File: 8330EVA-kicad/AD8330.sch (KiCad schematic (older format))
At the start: 2 parts, among them U1 AD8131, U3 AD8330

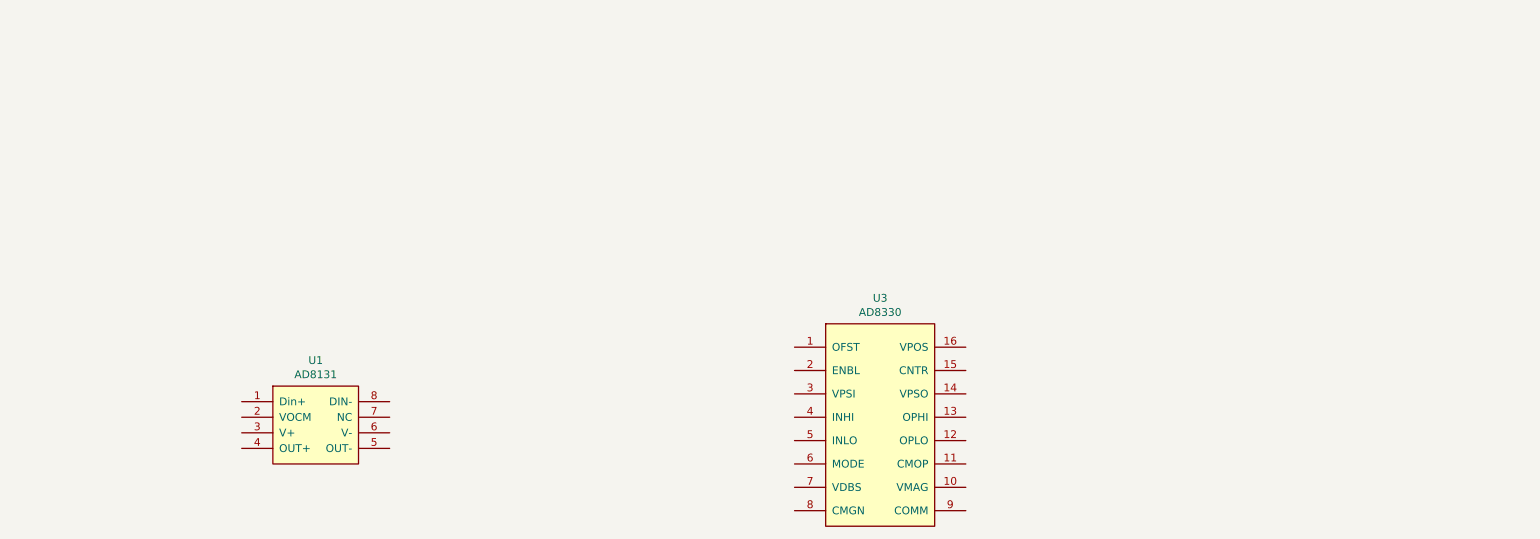
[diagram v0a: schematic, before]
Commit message: 完成AD8131单端转差分放大原理图绘制
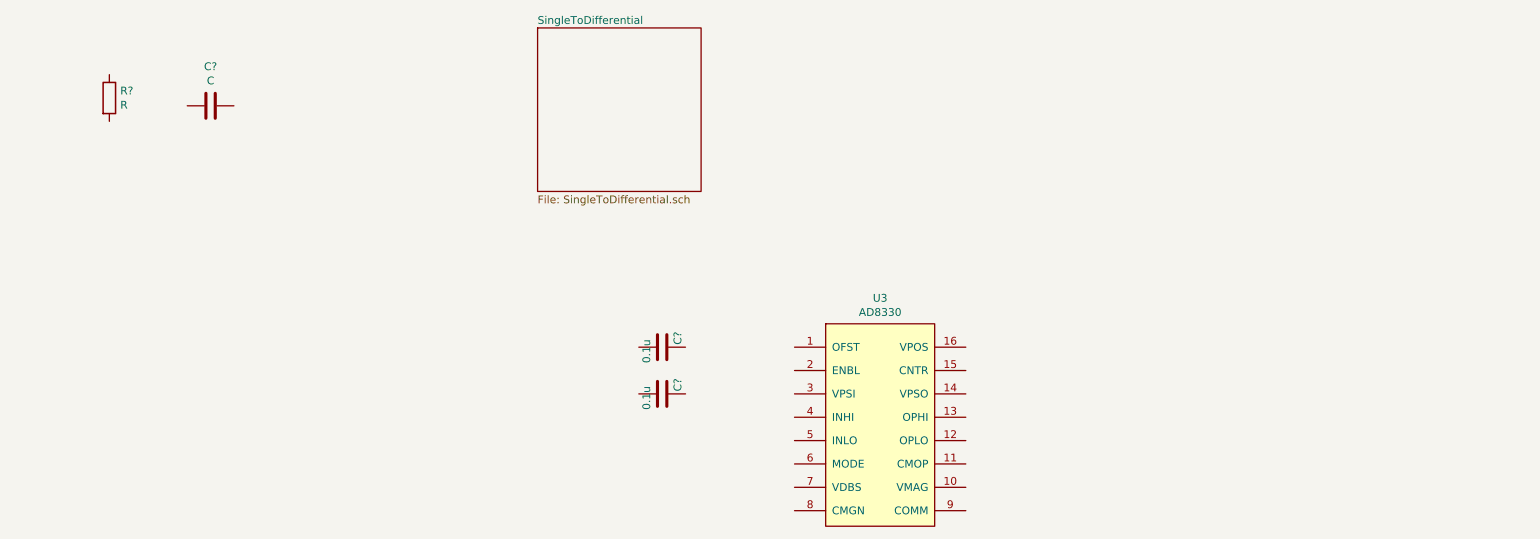
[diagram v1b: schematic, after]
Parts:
- removed U1: AD8131, Package_SO:SOIC-8_3.9x4.9mm_P1.27mm, symbol 8330_EVA-extra:AD8131
- added C?: C, symbol Device:C
- added C? (x2): 0.1u, symbol Device:C
- added R?: R, symbol Device:R
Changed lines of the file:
@@
 $Descr A4 11693 8268
 encoding utf-8
-Sheet 3 3
+Sheet 3 5
 Title ""
 Date ""
@@
 $EndComp
 $Comp
-L 8330_EVA-extra:AD8131 U1
-U 1 1 5BF81695
-P 2850 3250
-F 0 "U1" H 2825 3665 50  0000 C CNN
-F 1 "AD8131" H 2825 3574 50  0000 C CNN
-F 2 "Package_SO:SOIC-8_3.9x4.9mm_P1.27mm" H 3000 2850 50  0001 C CNN
-F 3 "https://www.analog.com/media/en/technical-documentation/data-sheets/AD8131.pdf" H 3000 2750 50  0001 C CNN
-	1    2850 3250
+L Device:R R?
+U 1 1 5BF9B361
+P 1500 1150
+F 0 "R?" H 1570 1196 50  0000 L CNN
+F 1 "R" H 1570 1105 50  0000 L CNN
+F 2 "" V 1430 1150 50  0001 C CNN
+F 3 "~" H 1500 1150 50  0001 C CNN
+	1    1500 1150
 	1    0    0    -1
 $EndComp
+$Comp
+L Device:C C?
+U 1 1 5BF9B6CC
+P 2150 1200
+F 0 "C?" V 1898 1200 50  0000 C CNN
+F 1 "C" V 1989 1200 50  0000 C CNN
+F 2 "" H 2188 1050 50  0001 C CNN
+F 3 "~" H 2150 1200 50  0001 C CNN
+	1    2150 1200
+	0    1    1    0
+$EndComp
+$Comp
+L Device:C C?
+U 1 1 5BFA5F5C
+P 5050 2750
+F 0 "C?" H 5150 2650 50  0000 R CNN
+F 1 "0.1u" H 5100 2850 50  0000 R CNN
+F 2 "" H 5088 2600 50  0001 C CNN
+F 3 "~" H 5050 2750 50  0001 C CNN
+	1    5050 2750
+	0    -1   -1   0
+$EndComp
+$Comp
+L Device:C C?
+U 1 1 5BFA682C
+P 5050 3050
+F 0 "C?" H 5150 2950 50  0000 R CNN
+F 1 "0.1u" H 5100 3150 50  0000 R CNN
+F 2 "" H 5088 2900 50  0001 C CNN
+F 3 "~" H 5050 3050 50  0001 C CNN
+	1    5050 3050
+	0    -1   -1   0
+$EndComp
+$Sheet
+S 4250 700  1050 1050
+U 5BFB4FFD
+F0 "SingleToDifferential" 50
+F1 "SingleToDifferential.sch" 50
+$EndSheet
 $EndSCHEMATC

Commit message: 完成AD8330 VGA电路原理图的绘制
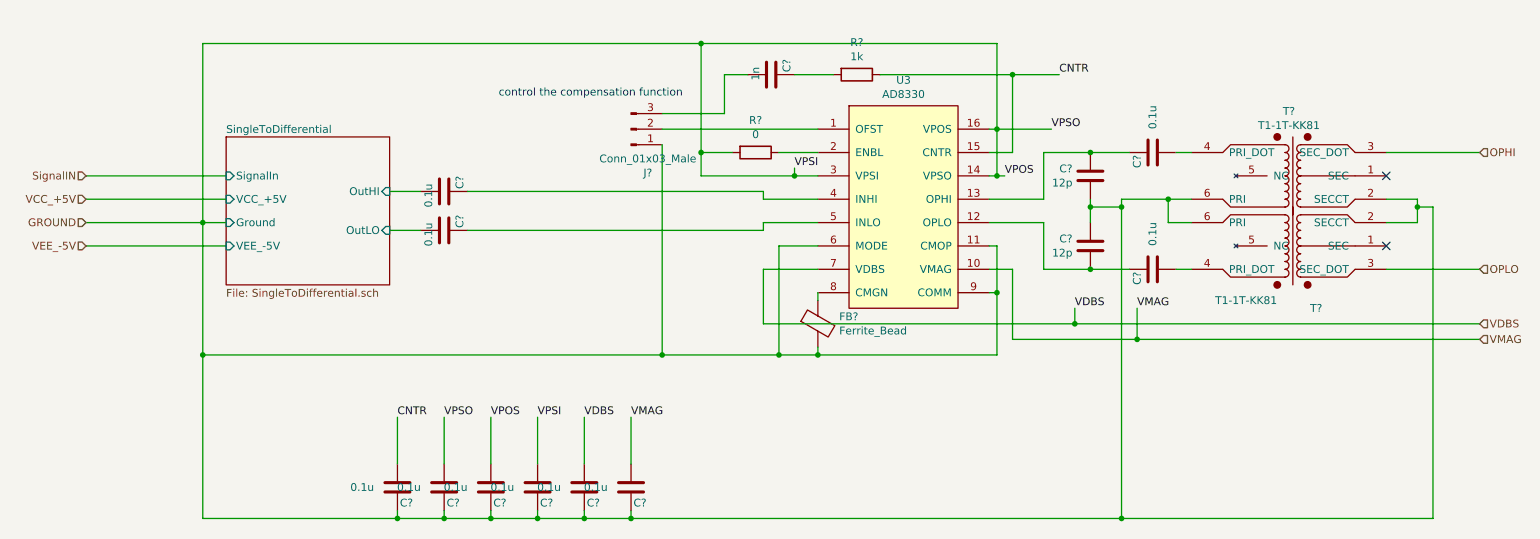
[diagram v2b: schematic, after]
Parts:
- removed C?: C, symbol Device:C
- removed C?: 0.1u, symbol Device:C
- added C? (x9): 0.1u, symbol Device:C
- added C? (x2): 12p, symbol Device:C
- added C?: 1n, symbol Device:C
- added FB?: Ferrite_Bead, symbol Device:Ferrite_Bead
- added J?: Conn_01x03_Male, symbol Connector:Conn_01x03_Male
- added R?: 1k, symbol Device:R
- added T? (x2): T1-1T-KK81, symbol 8330_EVA-extra:T1-1T-KK81
- R?: value R -> 0
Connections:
- net at U3.1 (OFST): now also J?.2 (Pin_2)
- net VMAG: now reaches U3.10 (VMAG)
- net VMAG: now also C?.1
- net GROUND: now reaches U3.11 (CMOP)
- net GROUND: now also R?.2, U3.14 (VPSO), U3.16 (VPOS), U3.3 (VPSI), U3.6 (MODE), U3.9 (COMM), C?.1, C?.1, C?.1, C?.1, C?.2, C?.2, C?.2, C?.2, C?.2, C?.2, C?.2, FB?.2, J?.1 (Pin_1), T?.2 (SECCT), T?.2 (SECCT), T?.6 (PRI), T?.6 (PRI)
- net at U3.12 (OPLO): now also C?.1, C?.2
- net at U3.13 (OPHI): now also C?.2, C?.2
- net CNTR: now reaches U3.15 (CNTR)
- net CNTR: now also C?.1, R?.1
- net at U3.2 (ENBL): now also R?.1
- net at U3.4 (INHI): now also C?.2
- net at U3.5 (INLO): now also C?.2
- net VDBS: now reaches U3.7 (VDBS)
- net VDBS: now also C?.1
- net at U3.8 (CMGN): now also FB?.1
- net SingleToDifferential/OutLO: now reaches C?.1
- new net: C?.1, T?.4 (PRI_DOT) (x2)
- new net: C?.1, J?.3 (Pin_3)
- new net: C?.2, R?.2
- new net OPHI: T?.3 (SEC_DOT)
- new net OPLO: T?.3 (SEC_DOT)
- new net SingleToDifferential/OutHI: C?.1
- no-connect marks 0 -> 2
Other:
- note added: "control the compensation function\n"
- moved on the sheet: C?, R?, U3

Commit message: 修复若干ERC未连接错误
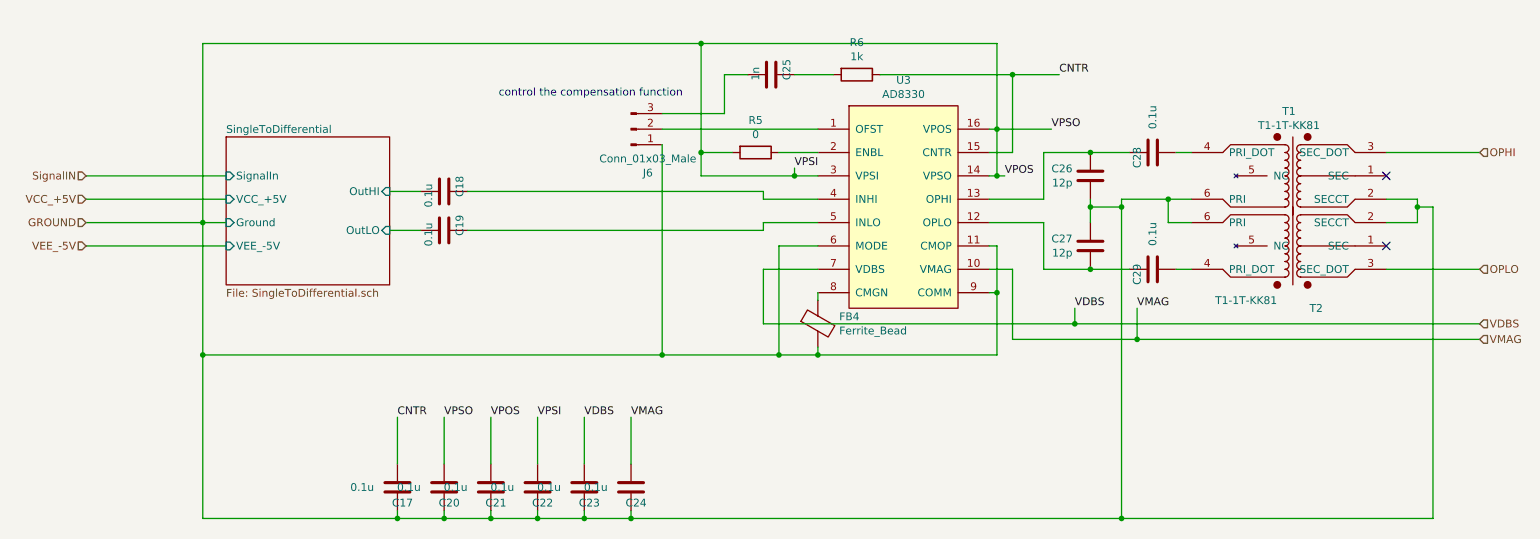
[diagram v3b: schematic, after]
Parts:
- gave numbers to parts that had none: 19
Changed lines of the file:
@@
 $EndComp
 $Comp
-L Device:R R?
+L Device:R R5
 U 1 1 5BF9B361
 P 5650 1500
-F 0 "R?" V 5443 1500 50  0000 C CNN
+F 0 "R5" V 5443 1500 50  0000 C CNN
 F 1 "0" V 5534 1500 50  0000 C CNN
 F 2 "" V 5580 1500 50  0001 C CNN
@@
 $EndComp
 $Comp
-L Device:C C?
+L Device:C C19
 U 1 1 5BFA682C
 P 3650 2000
-F 0 "C?" H 3750 1900 50  0000 R CNN
+F 0 "C19" H 3750 1900 50  0000 R CNN
 F 1 "0.1u" H 3700 2100 50  0000 R CNN
 F 2 "" H 3688 1850 50  0001 C CNN
@@
 	5700 1950 6050 1950
 $Comp
-L Device:C C?
+L Device:C C18
 U 1 1 5BFC8B3F
 P 3650 1750
-F 0 "C?" H 3750 1650 50  0000 R CNN
+F 0 "C18" H 3750 1650 50  0000 R CNN
 F 1 "0.1u" H 3700 1850 50  0000 R CNN
 F 2 "" H 3688 1600 50  0001 C CNN
@@
 	7500 1950 7500 2250
 $Comp
-L Device:C C?
+L Device:C C26
 U 1 1 5BFD0258
 P 7800 1650
-F 0 "C?" H 7685 1604 50  0000 R CNN
+F 0 "C26" H 7685 1604 50  0000 R CNN
 F 1 "12p" H 7685 1695 50  0000 R CNN
 F 2 "" H 7838 1500 50  0001 C CNN
@@
 $EndComp
 $Comp
-L Device:C C?
+L Device:C C27
 U 1 1 5BFD06D1
 P 7800 2100
-F 0 "C?" H 7685 2054 50  0000 R CNN
+F 0 "C27" H 7685 2054 50  0000 R CNN
 F 1 "12p" H 7685 2145 50  0000 R CNN
 F 2 "" H 7838 1950 50  0001 C CNN
@@
 	7800 1850 7800 1950
 $Comp
-L 8330_EVA-extra:T1-1T-KK81 T?
+L 8330_EVA-extra:T1-1T-KK81 T1
 U 1 1 5BFDF9EF
 P 9100 1650
-F 0 "T?" H 9075 2065 50  0000 C CNN
+F 0 "T1" H 9075 2065 50  0000 C CNN
 F 1 "T1-1T-KK81" H 9075 1974 50  0000 C CNN
 F 2 "" H 9690 1690 50  0001 C CNN
@@
 $EndComp
 $Comp
-L 8330_EVA-extra:T1-1T-KK81 T?
+L 8330_EVA-extra:T1-1T-KK81 T2
 U 1 1 5BFE14B7
 P 9100 2100
-F 0 "T?" H 9250 2500 50  0000 C CNN
+F 0 "T2" H 9250 2500 50  0000 C CNN
 F 1 "T1-1T-KK81" H 8800 2450 50  0000 C CNN
 F 2 "" H 9690 2140 50  0001 C CNN
@@
 Connection ~ 8000 1850
 Wire Wire Line
-	9700 1800 9900 1800
-Wire Wire Line
 	9900 1950 9700 1950
 Wire Wire Line
@@
 Connection ~ 7200 1350
 $Comp
-L Connector:Conn_01x03_Male J?
+L Connector:Conn_01x03_Male J6
 U 1 1 5C005F86
 P 4850 1350
-F 0 "J?" H 4958 1631 50  0000 C CNN
+F 0 "J6" H 4958 1631 50  0000 C CNN
 F 1 "Conn_01x03_Male" H 4958 1540 50  0000 C CNN
 F 2 "" H 4850 1350 50  0001 C CNN
@@
 	5050 1450 5050 2800
 $Comp
-L Device:R R?
+L Device:R R6
 U 1 1 5C01343E
 P 6300 1000
-F 0 "R?" V 6093 1000 50  0000 C CNN
+F 0 "R6" V 6093 1000 50  0000 C CNN
 F 1 "1k" V 6184 1000 50  0000 C CNN
 F 2 "" V 6230 1000 50  0001 C CNN
@@
 $EndComp
 $Comp
-L Device:C C?
+L Device:C C25
 U 1 1 5C01399A
 P 5750 1000
-F 0 "C?" H 5850 900 50  0000 R CNN
+F 0 "C25" H 5850 900 50  0000 R CNN
 F 1 "1n" H 5800 1100 50  0000 R CNN
 F 2 "" H 5788 850 50  0001 C CNN
@@
 control the compensation function\n
 $Comp
-L Device:Ferrite_Bead FB?
+L Device:Ferrite_Bead FB4
 U 1 1 5C01A12D
 P 6050 2600
-F 0 "FB?" H 6187 2646 50  0000 L CNN
+F 0 "FB4" H 6187 2646 50  0000 L CNN
 F 1 "Ferrite_Bead" H 6187 2555 50  0000 L CNN
 F 2 "" V 5980 2600 50  0001 C CNN
@@
 	5900 1650 6050 1650
 $Comp
-L Device:C C?
+L Device:C C21
 U 1 1 5C02ECCD
 P 3950 3650
-F 0 "C?" H 4050 3550 50  0000 R CNN
+F 0 "C21" H 4050 3550 50  0000 R CNN
 F 1 "0.1u" H 3800 3650 50  0000 R CNN
 F 2 "" H 3988 3500 50  0001 C CNN
@@
 $EndComp
 $Comp
-L Device:C C?
+L Device:C C22
 U 1 1 5C030FD6
 P 4250 3650
-F 0 "C?" H 4350 3550 50  0000 R CNN
+F 0 "C22" H 4350 3550 50  0000 R CNN
 F 1 "0.1u" H 4100 3650 50  0000 R CNN
 F 2 "" H 4288 3500 50  0001 C CNN
@@
 $EndComp
 $Comp
-L Device:C C?
+L Device:C C23
 U 1 1 5C0312A5
 P 4550 3650
-F 0 "C?" H 4650 3550 50  0000 R CNN
+F 0 "C23" H 4650 3550 50  0000 R CNN
 F 1 "0.1u" H 4400 3650 50  0000 R CNN
 F 2 "" H 4588 3500 50  0001 C CNN
@@
 $EndComp
 $Comp
-L Device:C C?
+L Device:C C24
 U 1 1 5C031714
 P 4850 3650
-F 0 "C?" H 4950 3550 50  0000 R CNN
+F 0 "C24" H 4950 3550 50  0000 R CNN
 F 1 "0.1u" H 4700 3650 50  0000 R CNN
 F 2 "" H 4888 3500 50  0001 C CNN
@@
 $EndComp
 $Comp
-L Device:C C?
+L Device:C C20
 U 1 1 5C031A2F
 P 3650 3650
-F 0 "C?" H 3750 3550 50  0000 R CNN
+F 0 "C20" H 3750 3550 50  0000 R CNN
 F 1 "0.1u" H 3500 3650 50  0000 R CNN
 F 2 "" H 3688 3500 50  0001 C CNN
@@
 $EndComp
 $Comp
-L Device:C C?
+L Device:C C17
 U 1 1 5C031D96
 P 3350 3650
-F 0 "C?" H 3450 3550 50  0000 R CNN
+F 0 "C17" H 3450 3550 50  0000 R CNN
 F 1 "0.1u" H 3200 3650 50  0000 R CNN
 F 2 "" H 3388 3500 50  0001 C CNN
@@
 NoConn ~ 9700 2100
 $Comp
-L Device:C C?
+L Device:C C28
 U 1 1 5C087144
 P 8200 1500
-F 0 "C?" H 8300 1400 50  0000 R CNN
+F 0 "C28" H 8300 1400 50  0000 R CNN
 F 1 "0.1u" H 8050 1500 50  0000 R CNN
 F 2 "" H 8238 1350 50  0001 C CNN
@@
 Connection ~ 7800 1500
 $Comp
-L Device:C C?
+L Device:C C29
 U 1 1 5C0A02D1
 P 8200 2250
-F 0 "C?" H 8300 2150 50  0000 R CNN
+F 0 "C29" H 8300 2150 50  0000 R CNN
 F 1 "0.1u" H 8050 2250 50  0000 R CNN
 F 2 "" H 8238 2100 50  0001 C CNN
@@
 EndData
 $EndBitmap
+Wire Wire Line
+	9700 1800 9900 1800
 $EndSCHEMATC

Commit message: 为变压器制作封装
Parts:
- C17, C18, C19, C20, C21, C22, C23, C24, C25, C26, C27, C28, C29: footprint (none) -> Capacitor_SMD:C_0603_1608Metric_Pad1.05x0.95mm_HandSolder
- FB4: footprint (none) -> Inductor_SMD:L_0805_2012Metric_Pad1.15x1.40mm_HandSolder
- J6: footprint (none) -> Connector_PinHeader_2.54mm:PinHeader_1x03_P2.54mm_Vertical
- R5, R6: footprint (none) -> Resistor_SMD:R_0805_2012Metric_Pad1.15x1.40mm_HandSolder
- T1, T2: footprint (none) -> 8330EVA-footprint-extra:Mini_Circuit_RF_Transformer_SO6
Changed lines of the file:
@@
 F 0 "R5" V 5443 1500 50  0000 C CNN
 F 1 "0" V 5534 1500 50  0000 C CNN
-F 2 "" V 5580 1500 50  0001 C CNN
+F 2 "Resistor_SMD:R_0805_2012Metric_Pad1.15x1.40mm_HandSolder" V 5580 1500 50  0001 C CNN
 F 3 "~" H 5650 1500 50  0001 C CNN
 	1    5650 1500
@@
 F 0 "C19" H 3750 1900 50  0000 R CNN
 F 1 "0.1u" H 3700 2100 50  0000 R CNN
-F 2 "" H 3688 1850 50  0001 C CNN
+F 2 "Capacitor_SMD:C_0603_1608Metric_Pad1.05x0.95mm_HandSolder" H 3688 1850 50  0001 C CNN
 F 3 "~" H 3650 2000 50  0001 C CNN
 	1    3650 2000
@@
 F 0 "C18" H 3750 1650 50  0000 R CNN
 F 1 "0.1u" H 3700 1850 50  0000 R CNN
-F 2 "" H 3688 1600 50  0001 C CNN
+F 2 "Capacitor_SMD:C_0603_1608Metric_Pad1.05x0.95mm_HandSolder" H 3688 1600 50  0001 C CNN
 F 3 "~" H 3650 1750 50  0001 C CNN
 	1    3650 1750
@@
 F 0 "C26" H 7685 1604 50  0000 R CNN
 F 1 "12p" H 7685 1695 50  0000 R CNN
-F 2 "" H 7838 1500 50  0001 C CNN
+F 2 "Capacitor_SMD:C_0603_1608Metric_Pad1.05x0.95mm_HandSolder" H 7838 1500 50  0001 C CNN
 F 3 "~" H 7800 1650 50  0001 C CNN
 	1    7800 1650
@@
 F 0 "C27" H 7685 2054 50  0000 R CNN
 F 1 "12p" H 7685 2145 50  0000 R CNN
-F 2 "" H 7838 1950 50  0001 C CNN
+F 2 "Capacitor_SMD:C_0603_1608Metric_Pad1.05x0.95mm_HandSolder" H 7838 1950 50  0001 C CNN
 F 3 "~" H 7800 2100 50  0001 C CNN
 	1    7800 2100
@@
 F 0 "T1" H 9075 2065 50  0000 C CNN
 F 1 "T1-1T-KK81" H 9075 1974 50  0000 C CNN
-F 2 "" H 9690 1690 50  0001 C CNN
+F 2 "8330EVA-footprint-extra:Mini_Circuit_RF_Transformer_SO6" H 9690 1690 50  0001 C CNN
 F 3 "https://ww3.minicircuits.com/pdfs/T1-1T-KK81.pdf" H 9100 1250 50  0001 C CNN
 	1    9100 1650
@@
 F 0 "T2" H 9250 2500 50  0000 C CNN
 F 1 "T1-1T-KK81" H 8800 2450 50  0000 C CNN
-F 2 "" H 9690 2140 50  0001 C CNN
+F 2 "8330EVA-footprint-extra:Mini_Circuit_RF_Transformer_SO6" H 9690 2140 50  0001 C CNN
 F 3 "https://ww3.minicircuits.com/pdfs/T1-1T-KK81.pdf" H 9100 1700 50  0001 C CNN
 	1    9100 2100
@@
 F 0 "J6" H 4958 1631 50  0000 C CNN
 F 1 "Conn_01x03_Male" H 4958 1540 50  0000 C CNN
-F 2 "" H 4850 1350 50  0001 C CNN
+F 2 "Connector_PinHeader_2.54mm:PinHeader_1x03_P2.54mm_Vertical" H 4850 1350 50  0001 C CNN
 F 3 "~" H 4850 1350 50  0001 C CNN
 	1    4850 1350
@@
 F 0 "R6" V 6093 1000 50  0000 C CNN
 F 1 "1k" V 6184 1000 50  0000 C CNN
-F 2 "" V 6230 1000 50  0001 C CNN
+F 2 "Resistor_SMD:R_0805_2012Metric_Pad1.15x1.40mm_HandSolder" V 6230 1000 50  0001 C CNN
 F 3 "~" H 6300 1000 50  0001 C CNN
 	1    6300 1000
@@
 F 0 "C25" H 5850 900 50  0000 R CNN
 F 1 "1n" H 5800 1100 50  0000 R CNN
-F 2 "" H 5788 850 50  0001 C CNN
+F 2 "Capacitor_SMD:C_0603_1608Metric_Pad1.05x0.95mm_HandSolder" H 5788 850 50  0001 C CNN
 F 3 "~" H 5750 1000 50  0001 C CNN
 	1    5750 1000
@@
 F 0 "FB4" H 6187 2646 50  0000 L CNN
 F 1 "Ferrite_Bead" H 6187 2555 50  0000 L CNN
-F 2 "" V 5980 2600 50  0001 C CNN
+F 2 "Inductor_SMD:L_0805_2012Metric_Pad1.15x1.40mm_HandSolder" V 5980 2600 50  0001 C CNN
 F 3 "~" H 6050 2600 50  0001 C CNN
 	1    6050 2600
@@
 F 0 "C21" H 4050 3550 50  0000 R CNN
 F 1 "0.1u" H 3800 3650 50  0000 R CNN
-F 2 "" H 3988 3500 50  0001 C CNN
+F 2 "Capacitor_SMD:C_0603_1608Metric_Pad1.05x0.95mm_HandSolder" H 3988 3500 50  0001 C CNN
 F 3 "~" H 3950 3650 50  0001 C CNN
 	1    3950 3650
@@
 F 0 "C22" H 4350 3550 50  0000 R CNN
 F 1 "0.1u" H 4100 3650 50  0000 R CNN
-F 2 "" H 4288 3500 50  0001 C CNN
+F 2 "Capacitor_SMD:C_0603_1608Metric_Pad1.05x0.95mm_HandSolder" H 4288 3500 50  0001 C CNN
 F 3 "~" H 4250 3650 50  0001 C CNN
 	1    4250 3650
@@
 F 0 "C23" H 4650 3550 50  0000 R CNN
 F 1 "0.1u" H 4400 3650 50  0000 R CNN
-F 2 "" H 4588 3500 50  0001 C CNN
+F 2 "Capacitor_SMD:C_0603_1608Metric_Pad1.05x0.95mm_HandSolder" H 4588 3500 50  0001 C CNN
 F 3 "~" H 4550 3650 50  0001 C CNN
 	1    4550 3650
@@
 F 0 "C24" H 4950 3550 50  0000 R CNN
 F 1 "0.1u" H 4700 3650 50  0000 R CNN
-F 2 "" H 4888 3500 50  0001 C CNN
+F 2 "Capacitor_SMD:C_0603_1608Metric_Pad1.05x0.95mm_HandSolder" H 4888 3500 50  0001 C CNN
 F 3 "~" H 4850 3650 50  0001 C CNN
 	1    4850 3650
@@
 F 0 "C20" H 3750 3550 50  0000 R CNN
 F 1 "0.1u" H 3500 3650 50  0000 R CNN
-F 2 "" H 3688 3500 50  0001 C CNN
+F 2 "Capacitor_SMD:C_0603_1608Metric_Pad1.05x0.95mm_HandSolder" H 3688 3500 50  0001 C CNN
 F 3 "~" H 3650 3650 50  0001 C CNN
 	1    3650 3650
@@
 F 0 "C17" H 3450 3550 50  0000 R CNN
 F 1 "0.1u" H 3200 3650 50  0000 R CNN
-F 2 "" H 3388 3500 50  0001 C CNN
+F 2 "Capacitor_SMD:C_0603_1608Metric_Pad1.05x0.95mm_HandSolder" H 3388 3500 50  0001 C CNN
 F 3 "~" H 3350 3650 50  0001 C CNN
 	1    3350 3650
@@
 F 0 "C28" H 8300 1400 50  0000 R CNN
 F 1 "0.1u" H 8050 1500 50  0000 R CNN
-F 2 "" H 8238 1350 50  0001 C CNN
+F 2 "Capacitor_SMD:C_0603_1608Metric_Pad1.05x0.95mm_HandSolder" H 8238 1350 50  0001 C CNN
 F 3 "~" H 8200 1500 50  0001 C CNN
 	1    8200 1500
@@
 F 0 "C29" H 8300 2150 50  0000 R CNN
 F 1 "0.1u" H 8050 2250 50  0000 R CNN
-F 2 "" H 8238 2100 50  0001 C CNN
+F 2 "Capacitor_SMD:C_0603_1608Metric_Pad1.05x0.95mm_HandSolder" H 8238 2100 50  0001 C CNN
 F 3 "~" H 8200 2250 50  0001 C CNN
 	1    8200 2250
